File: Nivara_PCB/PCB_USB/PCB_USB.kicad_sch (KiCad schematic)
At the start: 6 parts, among them J1 PINHD_2x2_Male, U1 GT-USB-7010ASV

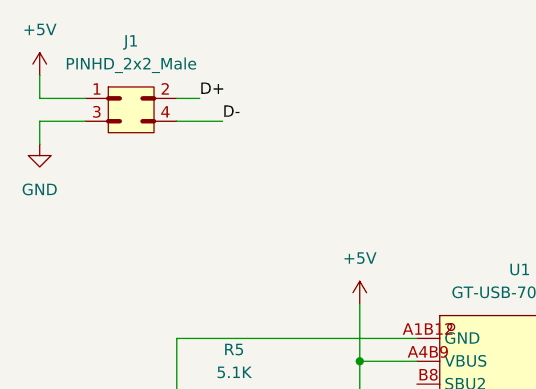
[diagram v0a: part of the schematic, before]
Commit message: Cambios en dimensiones de nivara PCB
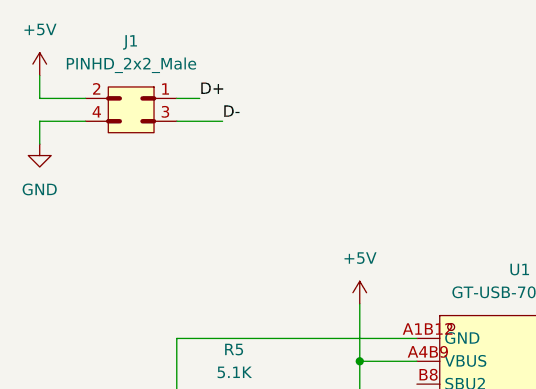
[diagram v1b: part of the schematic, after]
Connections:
- net +5V: now also J1.2; no longer J1.1
- net D+: now also J1.1; no longer J1.2
- net D-: now also J1.3; no longer J1.4
- net GND: now also J1.4; no longer J1.3
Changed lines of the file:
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@@
 		(lib_id "PCM_SL_Pin_Headers:PINHD_2x2_Male")
 		(at 59.69 40.64 0)
+		(mirror y)
 		(unit 1)
 		(exclude_from_sim no)
@@
 		(on_board yes)
 		(dnp no)
-		(fields_autoplaced yes)
 		(property "Reference" "J1"
 			(at 59.69 33.02 0)
@@
 		)
 		(property "Datasheet" ""
-			(at 58.42 33.02 0)
+			(at 60.96 33.02 0)
 			(effects
 				(font

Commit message: TERMINACIONES Y AJUSTES FINALES
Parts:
- removed D2: IR26-21C_L110_TR8, LED_SMD:LED_1206_3216Metric, symbol LED:IR26-21C_L110_TR8
- added D5: LED, LED_SMD:LED_0603_1608Metric, symbol EasyEDA:LED
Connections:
- net +5V: now also D5.2 (A)
- net D+: now also J1.3; no longer J1.1
- net D-: now also J1.1; no longer J1.3
- net at R6.2: now also D5.1 (K)
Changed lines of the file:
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@@
+	(wire
+		(pts
+			(xy 64.77 39.37) (xy 73.66 39.37)
+		)
+		(stroke
+			(width 0)
+			(type default)
+		)
+	)
 	(wire
 		(pts
@@
 	(wire
 		(pts
-			(xy 64.77 39.37) (xy 67.31 39.37)
-		)
-		(stroke
-			(width 0)
-			(type default)
-		)
-	)
-	(wire
-		(pts
 			(xy 49.53 44.45) (xy 49.53 41.91)
 		)
@@
 	(wire
 		(pts
-			(xy 64.77 41.91) (xy 69.85 41.91)
-		)
-		(stroke
-			(width 0)
-			(type default)
-		)
-	)
-	(wire
-		(pts
 			(xy 85.09 68.58) (xy 85.09 82.55)
 		)
@@
 		)
 	)
+	(wire
+		(pts
+			(xy 64.77 41.91) (xy 68.58 41.91)
+		)
+		(stroke
+			(width 0)
+			(type default)
+		)
+	)
 	(label "D+"
-		(at 67.31 39.37 0)
+		(at 68.58 41.91 0)
 		(effects
 			(font
@@
 	)
 	(label "D-"
-		(at 69.85 41.91 0)
+		(at 73.66 39.37 0)
 		(effects
 			(font
@@
 	)
 	(symbol
+		(lib_id "EasyEDA:LED")
+		(at 80.01 82.55 0)
+		(unit 1)
+		(exclude_from_sim no)
+		(in_bom yes)
+		(on_board yes)
+		(dnp no)
+		(property "Reference" "D5"
+			(at 80.01 72.898 90)
+			(effects
+				(font
+					(size 1.27 1.27)
+				)
+				(justify right)
+			)
+		)
+		(property "Value" "LED"
+			(at 77.47 72.898 90)
+			(effects
+				(font
+					(size 1.27 1.27)
+				)
+				(justify right)
+			)
+		)
+		(property "Footprint" "LED_SMD:LED_0603_1608Metric"
+			(at 80.01 82.55 0)
+			(effects
+				(font
+					(size 1.27 1.27)
+				)
+				(hide yes)
+			)
+		)
+		(property "Datasheet" "https://www.lcsc.com/datasheet/C84263.pdf"
+			(at 80.01 82.55 0)
+			(effects
+				(font
+					(size 1.27 1.27)
+				)
+				(hide yes)
+			)
+		)
+		(property "Description" "Light emitting diode"
+			(at 80.01 82.55 0)
+			(effects
+				(font
+					(size 1.27 1.27)
+				)
+				(hide yes)
+			)
+		)
+		(property "Sim.Pins" "1=K 2=A"
+			(at 80.01 82.55 0)
+			(effects
+				(font
+					(size 1.27 1.27)
+				)
+				(hide yes)
+			)
+		)
+		(property "LCSC Part" "C84263"
+			(at 80.01 82.55 90)
+			(effects
+				(font
+					(size 1.27 1.27)
+				)
+				(hide yes)
+			)
+		)
+		(property "Part #" "NCD0603R1"
+			(at 80.01 82.55 90)
+			(effects
+				(font
+					(size 1.27 1.27)
+				)
+				(hide yes)
+			)
+		)
+		(pin "1"
+		)
+		(pin "2"
+		)
+		(instances
+			(project "PCB_USB"
+				(path "/337ea9b7-e69a-47dc-85a1-a69003190f09"
+					(reference "D5")
+					(unit 1)
+				)
+			)
+		)
+	)
+	(symbol
 		(lib_id "EasyEDA:R_0603")
 		(at 71.12 88.9 90)
@@
 					(unit 1)
 				)
-			)
-		)
-	)
-	(symbol
-		(lib_id "LED:IR26-21C_L110_TR8")
-		(at 80.01 82.55 0)
-		(unit 1)
-		(exclude_from_sim no)
-		(in_bom yes)
-		(on_board yes)
-		(dnp no)
-		(fields_autoplaced yes)
-		(property "Reference" "D2"
-			(at 78.4225 76.2 0)
-			(effects
-				(font
-					(size 1.27 1.27)
-				)
-			)
-		)
-		(property "Value" "IR26-21C_L110_TR8"
-			(at 78.4225 78.74 0)
-			(effects
-				(font
-					(size 1.27 1.27)
-				)
-			)
-		)
-		(property "Footprint" "LED_SMD:LED_1206_3216Metric"
-			(at 80.01 77.47 0)
-			(effects
-				(font
-					(size 1.27 1.27)
-				)
-				(hide yes)
-			)
-		)
-		(property "Datasheet" "http://www.everlight.com/file/ProductFile/IR26-21C-L110-TR8.pdf"
-			(at 80.01 82.55 0)
-			(effects
-				(font
-					(size 1.27 1.27)
-				)
-				(hide yes)
-			)
-		)
-		(property "Description" "940nm, 20 deg, Infrared LED, 1206"
-			(at 80.01 82.55 0)
-			(effects
-				(font
-					(size 1.27 1.27)
-				)
-				(hide yes)
-			)
-		)
-		(pin "2"
-		)
-		(pin "1"
-		)
-		(instances
-			(project ""
-				(path "/337ea9b7-e69a-47dc-85a1-a69003190f09"
-					(reference "D2")
-					(unit 1)
-				)
